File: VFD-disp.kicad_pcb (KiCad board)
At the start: 4 copper layers, 99.6 x 65.5 mm, 123 parts, among them J1 USB_C_Receptacle_USB2.0_14P, J2 Conn_02x03_Odd_Even, J4 Conn_02x03_Odd_Even, J5 Conn_02x03_Odd_Even, J6 Conn_02x03_Odd_Even, Q1 Q_NMOS_GDS, Q3 Q_NPN_BEC, SW1 SW_SPST, U1 ESP32-C6-WROOM-1, U10 TXS0104EPW, U11 MAX811TEUS-T, U12 MCP4728, U13 TPS2116DRL, U14 KF50BDT, U15 AT24CS01-STUM, U2 FUSB302B01MPX, U3 LM1117DT-3.3, U5 LM2576HVS-ADJ, U6 MAX1771xSA, U7 LM2576-5.0WU, U8 USBLC6-2P6, U9 DRV8837, Y1 Crystal

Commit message: Finish routing
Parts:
- moved C1 2.40 mm to (86.9, 244.4)
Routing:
- net BLANKING: track 6.38 -> 31.3 mm, vias 0 -> 2
- net VPP: track 91.5 -> 101.0 mm, vias 5 -> 7
- net +5V: track 14.3 -> 22.3 mm
- net GND: track 228.8 -> 223.6 mm, vias 109 -> 114
- net DATA_IN: track 20.7 -> 18.8 mm
- net BLUE7: track 21.0 -> 22.8 mm
- net CLOCK: track 37.3 -> 39.1 mm, vias 2 -> 3
- net F_PWM: track 65.3 -> 64.1 mm
- net Net-(HV5812WG2-OUT15): track 20.6 -> 19.6 mm
- net F: track 138.8 -> 137.8 mm
- net STROBE: track 42.4 -> 43.3 mm
- net RED7: track 23.8 -> 24.6 mm
- net GREEN3: track 65.4 -> 64.6 mm
- net GREEN7: track 44.2 -> 45.0 mm
- net Net-(HV5812WG2-OUT14): track 23.0 -> 23.6 mm
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
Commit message: Update schematic
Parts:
- removed C25, C6: 150uF, Capacitor_SMD:CP_Elec_5x4.5
- removed C29, C35, C5: 100nF, Capacitor_SMD:C_0805_2012Metric
- removed C7: 10uF, Capacitor_SMD:CP_Elec_5x4.5
- removed C8: 100nF, Capacitor_SMD:C_2220_5750Metric
- removed D1: B3100BE-13, Diode_SMD:D_SMB
- removed D6: BZV55B7V5, Diode_SMD:D_MiniMELF
- removed L1, L4: 100uH, Inductor_SMD:L_Bourns_SRP1038C_10.0x10.0mm
- removed Q1: Q_NMOS_GDS, Package_TO_SOT_SMD:TO-263-2
- removed Q3: Q_NPN_BEC, Package_TO_SOT_SMD:SOT-23
- removed R28, R3: 4.7k, Resistor_SMD:R_0805_2012Metric
- removed R29: 10k, Resistor_SMD:R_0805_2012Metric
- removed R30: 100k, Resistor_SMD:R_0805_2012Metric
- removed R4: 40m, Resistor_SMD:R_0805_2012Metric
- removed R44, R8: R, Resistor_SMD:R_0805_2012Metric
- removed R5: 2.7k, Resistor_SMD:R_0805_2012Metric
- removed R6: 1.2k, Resistor_SMD:R_0805_2012Metric
- removed RV3: 20k, Potentiometer_SMD:Potentiometer_Bourns_3269W_Vertical
- removed U12: MCP4728, Package_SO:MSOP-10_3x3mm_P0.5mm
- removed U13: TPS2116DRL, Package_TO_SOT_SMD:SOT-583-8
- removed U6: MAX1771xSA, Package_SO:SO-8_3.9x4.9mm_P1.27mm
- removed Y1: Crystal, Crystal:Crystal_SMD_HC49-SD
- added C34: 100nF, Capacitor_SMD:C_0805_2012Metric, F.Cu at (76.9, 200.3)
- added C42: 100nF, Capacitor_SMD:C_0805_2012Metric, F.Cu at (105.2, 218.9)
- added C43: 3.3nF, Capacitor_SMD:C_0805_2012Metric, F.Cu at (96.6, 222.8)
- added C44: 1nF, Capacitor_SMD:C_0805_2012Metric, F.Cu at (95.7, 220.1)
- added L2: 47uF, Inductor_SMD:L_Bourns_SRP1038C_10.0x10.0mm, F.Cu at (124.1, 228.8)
- added Q2: Q_NMOS_GDS, Package_TO_SOT_SMD:TO-252-2, F.Cu at (113.3, 224.7)
- added R10: 2.7k, Resistor_SMD:R_0805_2012Metric, F.Cu at (105.8, 232.3)
- added R11: 1.2k, Resistor_SMD:R_0805_2012Metric, F.Cu at (94.8, 231.5)
- added R12: R, Resistor_SMD:R_0805_2012Metric, F.Cu at (94.8, 228.1)
- added RV4: 20k, Potentiometer_SMD:Potentiometer_Bourns_3269W_Vertical, F.Cu at (99.9, 229.8)
- added U4: MCP4661-103E_ST, Package_SO:TSSOP-14_4.4x5mm_P0.65mm, F.Cu at (75.0, 204.3)
- C15: value C -> 10uF; footprint Capacitor_SMD:C_0805_2012Metric -> Capacitor_SMD:CP_Elec_5x4.5
- C16: value C -> 150uF; footprint Capacitor_SMD:C_0805_2012Metric -> Capacitor_SMD:CP_Elec_5x4.5
- D4: value SS24 -> B3100BE-13
- R13: value R -> 40m
- R14: value 10k -> 26k7
- R17: value 100k -> 10K
- R23: value 3.83k -> 100k
- R27: value 1k -> 56k2
- U7: value LM2576-5.0WU -> LM3478MA; footprint Package_TO_SOT_SMD:TO-263-5_TabPin3 -> Package_SO:SOIC-8_3.9x4.9mm_P1.27mm
- moved C9 74.6 mm to (123.7, 247.8), turned to -90 degrees
- moved D4 57.9 mm to (124.1, 239.3)
- moved U7 53.3 mm to (102.7, 223.5), turned to 0 degrees
- moved R27 41.9 mm to (97.7, 220.0)
- moved C16 29.9 mm to (129.8, 208.2), turned to 180 degrees
- moved C15 26.1 mm to (113.7, 231.4), turned to 0 degrees
- moved R13 24.7 mm to (106.8, 229.4), turned to 180 degrees
- moved R14 21.5 mm to (102.7, 218.9), turned to 90 degrees
- moved R24 21.4 mm to (66.4, 208.5), turned to 0 degrees
- moved R23 13.3 mm to (60.3, 209.2), turned to 0 degrees
- moved C38 7.85 mm to (61.8, 205.4)
- moved C39 7.85 mm to (61.8, 200.8)
- moved C40 7.85 mm to (61.3, 203.1)
- moved C41 7.85 mm to (57.0, 198.4)
- moved U14 7.85 mm to (52.9, 203.1)
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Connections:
- C15 pad 1: Net-(U1-GPIO1/ADC1_CH1/XTAL_32K_N) -> VPP
- C16 pad 1: Net-(U1-GPIO0/ADC1_CH0/XTAL_32K_P) -> VBUS
- C23 pad 1: VBUS -> Net-(U1-GPIO1/ADC1_CH1/XTAL_32K_N)
- C39 pad 1: Net-(U13-VIN2) -> Net-(U14-VO)
- C41 pad 1: Net-(U13-VIN2) -> Net-(U14-VO)
- C9 pad 1: Net-(U13-MODE) -> VPP
- D4 pad 1: Net-(D4-K) -> VPP
- D4 pad 2: GND -> Net-(D4-A)
- F4 pad 1: Net-(F4-Pad1) -> Net-(U14-VO)
- R13 pad 1: +3.3V -> Net-(Q2-S)
- R13 pad 2: /4728_RDY -> GND
- R14 pad 1: /NEG_LDAC -> Net-(U7-FA/SD)
- R23 pad 1: Net-(U13-MODE) -> VBUS
- R23 pad 2: Net-(U13-PR1) -> Net-(U1-GPIO1/ADC1_CH1/XTAL_32K_N)
- R24 pad 1: VBUS -> Net-(U1-GPIO1/ADC1_CH1/XTAL_32K_N)
- R24 pad 2: Net-(D6-K) -> GND
- R27 pad 1: Net-(U13-PR1) -> Net-(C43-Pad2)
- U1 pad 8: Net-(U1-GPIO0/ADC1_CH0/XTAL_32K_P) -> unconnected-(U1-GPIO0/ADC1_CH0/XTAL_32K_P-Pad8)
- U14 pad 3: Net-(U13-VIN2) -> Net-(U14-VO)
- U7 pad 1: VBUS -> Net-(Q2-S)
- U7 pad 2: Net-(D4-K) -> Net-(U7-COMP)
- U7 pad 3: GND -> Net-(U7-FB)
- U7 pad 4: Net-(U13-MODE) -> GND
- U7 pad 5: Net-(Q3-C) -> GND
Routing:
- net RX1: track 81.3 -> 0.00 mm, vias 1 -> 0
- net TX1: track 80.7 -> 0.00 mm, vias 1 -> 0
- net GND: track 223.6 -> 154.6 mm, vias 114 -> 92
- net FORWARD_DETECT: track 67.4 -> 2.09 mm, vias 1 -> 0
- net F_PWM: track 64.1 -> 0.00 mm, vias 4 -> 0
- net F_ADJ: track 59.6 -> 0.00 mm, vias 2 -> 0
- net Net-(U13-MODE): track 43.7 -> 0.00 mm
- net VBUS_ABOVE_TRESHOLD: track 43.7 -> 0.00 mm, vias 4 -> 0
- net /HV_EN: track 36.9 -> 0.00 mm, vias 4 -> 0
- net Net-(U6-FB): track 32.7 -> 0.00 mm, vias 2 -> 0
- net VPP: track 101.0 -> 73.0 mm, vias 7 -> 3
- net VBUS: track 49.3 -> 26.8 mm, vias 12 -> 6
- net Net-(U13-VIN2): track 21.1 -> 0.00 mm, vias 2 -> 0
- net +3.3V: track 108.0 -> 87.3 mm, vias 22 -> 17
- net HV_ADJ: track 20.7 -> 0.00 mm, vias 4 -> 0
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
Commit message: run autoroute
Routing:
- net GND: track 154.6 -> 253.2 mm
- net RX1: track 0.00 -> 78.8 mm, vias 0 -> 2
- net TX1: track 0.00 -> 76.7 mm, vias 0 -> 2
- net F_PWM: track 0.00 -> 64.9 mm, vias 0 -> 6
- net FORWARD_DETECT: track 2.09 -> 63.6 mm, vias 0 -> 2
- net SCL: track 43.0 -> 85.5 mm
- net Net-(U1-GPIO1/ADC1_CH1/XTAL_32K_N): track 3.98 -> 46.0 mm, vias 0 -> 2
- net SDA: track 42.9 -> 76.9 mm, vias 4 -> 6
- net HV_ADJ: track 0.00 -> 30.9 mm, vias 0 -> 4
- net VPP: track 73.0 -> 102.7 mm, vias 3 -> 5
- net +3.3V: track 87.3 -> 106.7 mm
- net Net-(D4-A): track 0.00 -> 17.6 mm
- net F_EN: track 99.1 -> 116.6 mm, vias 4 -> 5
- net Net-(Q2-S): track 0.00 -> 13.0 mm
- net Net-(U7-FB): track 0.00 -> 12.7 mm
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
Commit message: Finish routing
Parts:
- moved R14 1.18 mm to (101.5, 218.8)
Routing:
- net GND: track 253.2 -> 222.1 mm, vias 92 -> 103
- net VBUS: track 37.4 -> 42.2 mm, vias 6 -> 8
- net +3.3V: track 106.7 -> 105.1 mm
- net Net-(U7-FA/SD): track 4.25 -> 5.67 mm
- net HV_ADJ: track 30.9 -> 31.7 mm
- net Net-(Q2-G): track 4.15 -> 4.94 mm
- net Net-(D4-A): track 17.6 -> 18.4 mm
- net VPP: track 102.7 -> 103.2 mm, vias 5 -> 6

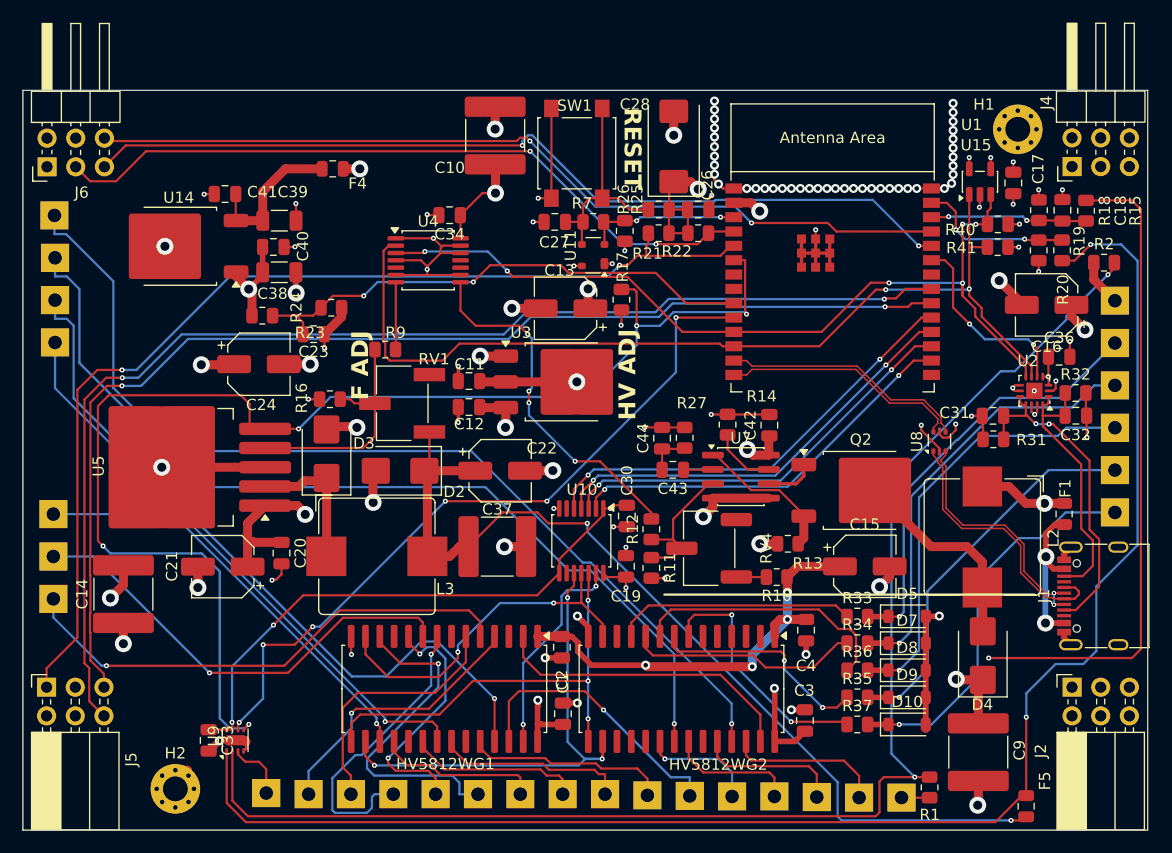
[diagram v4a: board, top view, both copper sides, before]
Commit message: Fix USB and heater traces
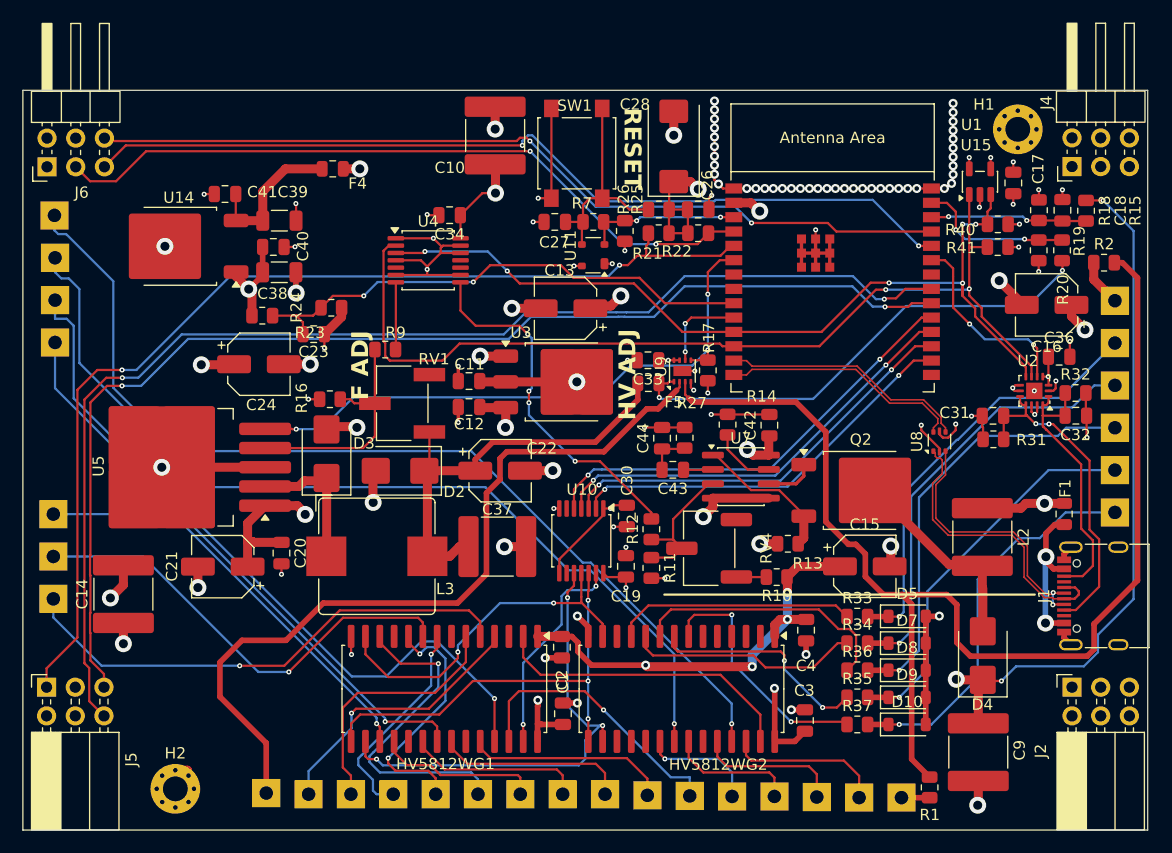
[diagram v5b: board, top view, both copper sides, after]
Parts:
- L2: value 47uF -> 47uH; footprint Inductor_SMD:L_Bourns_SRP1038C_10.0x10.0mm -> Capacitor_SMD:C_2220_5750Metric
- moved C33 51.4 mm to (94.5, 213.2), turned to 180 degrees
- moved U9 51.4 mm to (97.5, 214.1)
- moved F5 50.2 mm to (94.5, 215.2), turned to 0 degrees
- moved R17 9.89 mm to (99.8, 214.1)
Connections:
- R1 pad 2: Net-(U9-OUT1) -> Net-(U9-OUT2)
- R2 pad 2: Net-(U9-OUT1) -> Net-(U9-OUT2)
- U9 pad 2: Net-(U9-OUT1) -> Net-(IVLM3-5/1-F2)
- U9 pad 3: Net-(IVLM3-5/1-F2) -> Net-(U9-OUT2)
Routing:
- net Net-(U9-OUT1): track 125.1 -> 0.00 mm, vias 2 -> 0
- net Net-(U9-OUT2): track 0.00 -> 109.2 mm
- net F: track 137.8 -> 44.1 mm
- net Net-(IVLM3-5/1-F2): track 5.47 -> 69.9 mm
- net F_EN: track 116.6 -> 54.1 mm, vias 5 -> 3
- net F_PWM: track 64.9 -> 7.77 mm, vias 6 -> 2
- net +3.3V: track 105.1 -> 56.8 mm, vias 17 -> 16
- net Net-(D2-K): track 83.9 -> 38.1 mm, vias 2 -> 0
- net GND: track 222.1 -> 200.3 mm, vias 103 -> 105
- net RED6: track 26.3 -> 19.0 mm
- net VPP: track 103.2 -> 99.9 mm, vias 6 -> 7
- net USB_D+: track 24.1 -> 26.2 mm
- net USB_D-: track 22.4 -> 24.1 mm
- net RX2: track 107.8 -> 109.5 mm
- net TX2: track 104.1 -> 105.4 mm
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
